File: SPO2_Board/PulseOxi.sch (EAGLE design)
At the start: 45 parts, among them IC1 AFE4400RHAR

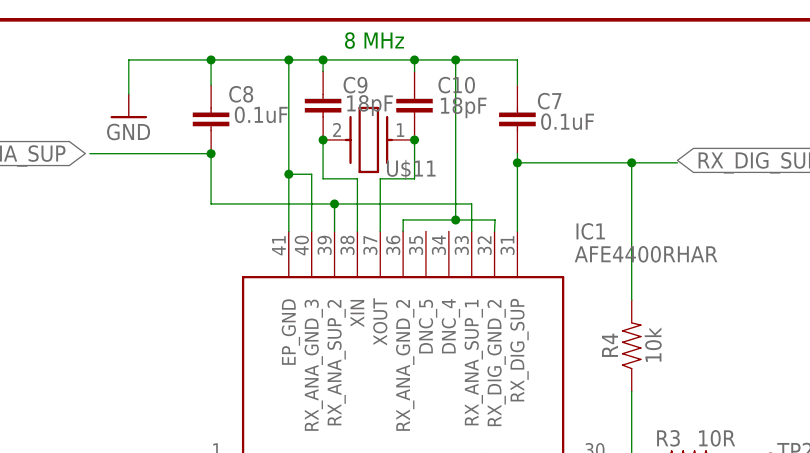
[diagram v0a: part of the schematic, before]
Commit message: Board Updates
All LEDs at same location
Separated analog and digital ground
Updated impedance components
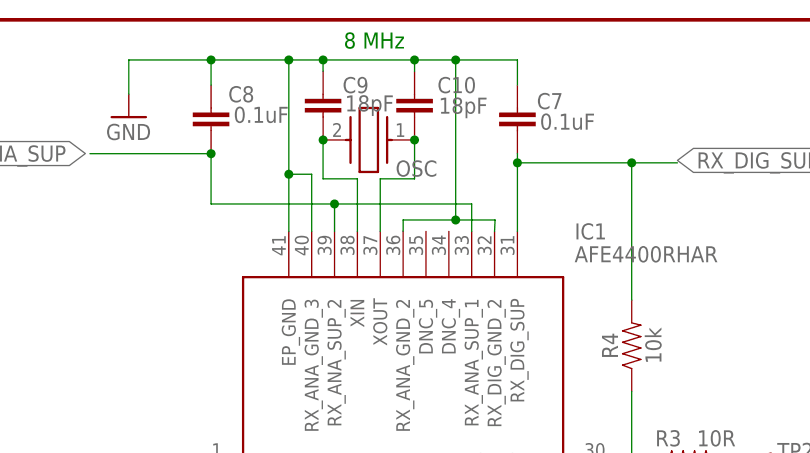
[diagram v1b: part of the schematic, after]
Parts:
- renumbered U$11 to OSC
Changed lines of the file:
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@@
 <part name="GND48" library="supply1" deviceset="GND" device=""/>
 <part name="P+12" library="supply1" deviceset="VCC" device=""/>
-<part name="U$11" library="ABM3-8.000MHZ-D2Y-T" deviceset="ABM3-8.000MHZ-D2Y-T" device=""/>
+<part name="OSC" library="ABM3-8.000MHZ-D2Y-T" deviceset="ABM3-8.000MHZ-D2Y-T" device=""/>
 <part name="X2" library="circuitects" deviceset="DB9" device=""/>
 <part name="GND32" library="supply1" deviceset="GND" device=""/>
@@
 <attribute name="VALUE" x="-22.7" y="-13.52" size="1.778" layer="96" rot="R90"/>
 </instance>
-<instance part="U$11" gate="G$1" x="46.99" y="102.87" smashed="yes" rot="R180">
+<instance part="OSC" gate="G$1" x="46.99" y="102.87" smashed="yes" rot="R180">
 <attribute name="NAME" x="49.53" y="100.584" size="1.778" layer="95" rot="R180"/>
 </instance>
@@
 <net name="N$16" class="0">
 <segment>
-<pinref part="U$11" gate="G$1" pin="2"/>
+<pinref part="OSC" gate="G$1" pin="2"/>
 <wire x1="36.83" y1="98.552" x2="36.83" y2="102.87" width="0.1524" layer="91"/>
 <junction x="36.83" y="102.87"/>
@@
 <net name="N$19" class="0">
 <segment>
-<pinref part="U$11" gate="G$1" pin="1"/>
+<pinref part="OSC" gate="G$1" pin="1"/>
 <pinref part="C10" gate="G$1" pin="1"/>
 <junction x="46.99" y="102.87"/>
